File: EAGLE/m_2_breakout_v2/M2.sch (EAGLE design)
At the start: 37 parts, among them X1 C-GRID-14-70543, X2 C-GRID-14-70543, X4 87758-0416

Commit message: Fixed everything about m2 board, just need optional switch rack
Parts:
- removed P_5V, P_ML_EN, P_MR_EN: LSP10, solpad:LSP10
- removed X3: (no value), con-molex:KK-156-2
- added 5V_M2, J_5V_HEX, J_GND_HEX, J_GND_SCH, J_LED_B, J_LED_B_D, J_LED_R, J_LED_R_D, J_ML_OUT1, J_ML_OUT1_D, J_MR_CAPS_GND, J_MR_OUT1, J_MR_OUT1_D, J_MR_PWM, J_MR_PWM_D: ARDUINO_HEADER_1X1_OCTAGON, ben_kramer:ARDUINO_HEADER_1X1_OCTAGON
- added 5V_RAIL: (no value), con-lsta:FE06-1
- added BATTERY, BREAKBEAM_IN: MOLEX_2_PIN, ben_kramer:MOLEX_2_PIN
- added BREAKBEAM_POT: POTENTIOMETER_1, ben_kramer:POTENTIOMETER_1
- added BREAKBEAM_RP: 10k, ben_kramer:RESISTOR_THROUGH_8MM
- added BREAKBEAM_RS: 1k, ben_kramer:RESISTOR_THROUGH_8MM
- added POSITIONING_LED: RGB_LED, ben_kramer:RGB_LED
- renumbered ML_DIODE_NOTE to MR_DIODE_NOT, SV3 to GND_RAIL
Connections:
- net N$3 renamed B5
- net N$6 renamed C7
- removed net GND_1: J_GND5.MP, MWII_L.3
- removed net N$14: C1.2, C2.1, IC1.GND
- removed net N$34: C1.1, C4.1, IC1.IN, X3-2.S, X4-2.S, X4-4.S
- removed net N$5: U$1.C6, X1-5.S
- removed net N$51: C4.2, GND_RAIL.1, GND_RAIL.2, GND_RAIL.3, GND_RAIL.4, GND_RAIL.5, GND_RAIL.6, X3-1.S, X4-1.S, X4-3.S
- new net 5V_HEX: HEX_INVERTER.VCC, J_5V_HEX.1
- new net BREAKBEAM_OUT: BREAKBEAM_IN.2, BREAKBEAM_RP.1, BREAKBEAM_RS.2, U$1.C6, X1-5.S
- new net GND_HEX: HEX_INVERTER.GND, J_GND_HEX.1
- new net GND_SCH: J_GND_SCH.1, SCHMITT_INVERTER.GND
- new net IN_GND: BATTERY.2, C1.2, C2.1, C4.2, GND_RAIL.1, GND_RAIL.2, GND_RAIL.3, GND_RAIL.4, GND_RAIL.5, GND_RAIL.6, IC1.GND, X4-1.S, X4-3.S
- new net LED_B: J_LED_B.1, POSITIONING_LED.B
- new net LED_R: J_LED_R.1, POSITIONING_LED.R
- new net M2_GND: BREAKBEAM_IN.1, BREAKBEAM_RP.2, J_GND5.MP, MWII_L.3
- new net ML_OUT1_D: J_ML_OUT1_D.1, TO_MOTOR_CONTROLLER.2
- new net MR_CAPS_GND: J_MR_CAPS_GND.1, MR_CAP.1, MR_CAP_NOT.1
- new net MR_OUT1_D: J_MR_OUT1_D.1, TO_MOTOR_CONTROLLER.5
- new net MR_PWM_D: HEX_INVERTER.6A, J_MR_PWM_D.1
- new net N$19: 5V_M2.1, U$1.V+, X1-1.S
- new net N$6: BREAKBEAM_POT.2, BREAKBEAM_RS.1
- new net VIN: BATTERY.1, C1.1, C4.1, IC1.IN, X4-2.S, X4-4.S
- net 5V: now also 5V_RAIL.1, 5V_RAIL.2, 5V_RAIL.3, 5V_RAIL.4, 5V_RAIL.5, 5V_RAIL.6, BREAKBEAM_POT.1; no longer HEX_INVERTER.VCC, P_5V.MP, U$1.V+, X1-1.S
- net B2: now also J_LED_B_D.1
- net B3: now also J_LED_R_D.1
- net GND: no longer HEX_INVERTER.GND, MR_CAP.1, MR_CAP_NOT.1, SCHMITT_INVERTER.GND
- net ML_EN: no longer P_ML_EN.MP
- net ML_OUT1: now also J_ML_OUT1.1; no longer TO_MOTOR_CONTROLLER.2
- net MR_EN: no longer P_MR_EN.MP
- net MR_OUT1: now also J_MR_OUT1.1; no longer TO_MOTOR_CONTROLLER.5
- net MR_PWM: now also J_MR_PWM.1; no longer HEX_INVERTER.6A
- net N$17: now also POSITIONING_LED.GND

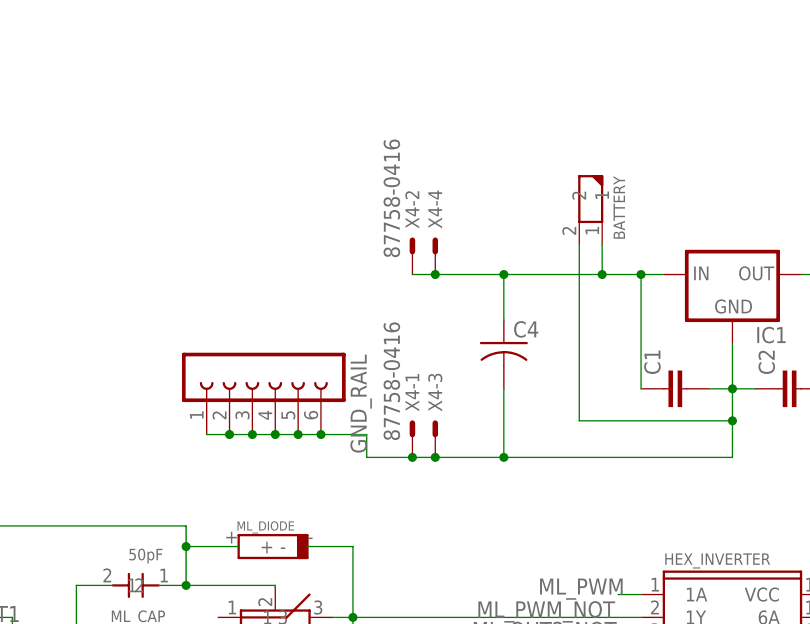
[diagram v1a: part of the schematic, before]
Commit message: Fixed headers out
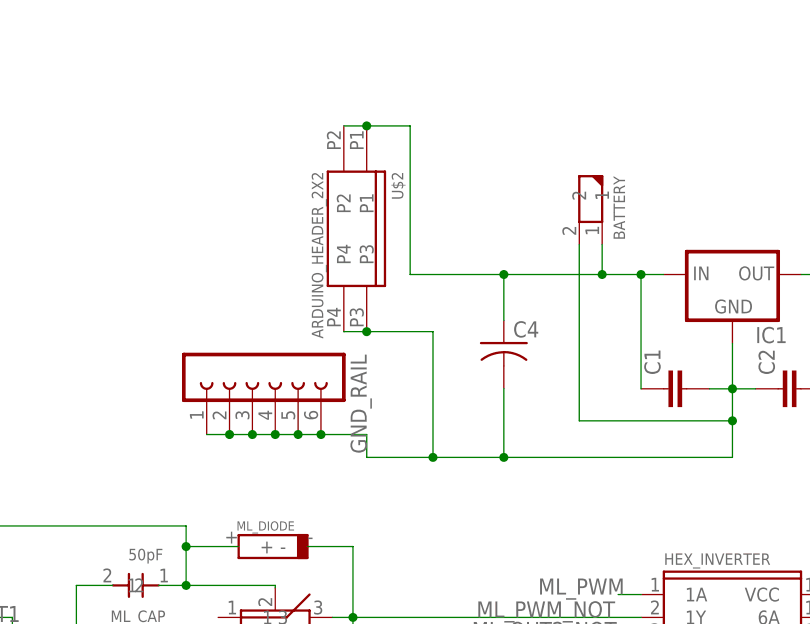
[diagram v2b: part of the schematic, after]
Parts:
- removed X4: 87758-0416, con-molex:87758-0416
- added U$2: ARDUINO_HEADER_2X2, ben_kramer:ARDUINO_HEADER_2X2
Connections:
- net IN_GND: now also U$2.P3, U$2.P4; no longer X4-1.S, X4-3.S
- net VIN: now also U$2.P1, U$2.P2; no longer X4-2.S, X4-4.S
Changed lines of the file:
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@@
 <part name="C2" library="capacitor-wima" deviceset="C" device="2,5-3"/>
 <part name="IC1" library="v-reg" deviceset="78MXXS" device=""/>
-<part name="X4" library="con-molex" deviceset="87758-0416" device=""/>
 <part name="MWII_L" library="con-lstb" deviceset="MA03-1" device=""/>
 <part name="MWII_R" library="con-lstb" deviceset="MA03-1" device=""/>
@@
 <part name="BREAKBEAM_RS" library="ben_kramer" deviceset="RESISTOR_THROUGH_8MM" device="" value="1k"/>
 <part name="BREAKBEAM_POT" library="ben_kramer" deviceset="POTENTIOMETER_1" device=""/>
+<part name="U$2" library="ben_kramer" deviceset="ARDUINO_HEADER_2X2" device=""/>
 </parts>
 <sheets>
@@
 <instance part="C2" gate="G$1" x="12.7" y="78.74" rot="R90"/>
 <instance part="IC1" gate="A" x="7.62" y="91.44"/>
-<instance part="X4" gate="-1" x="-27.94" y="73.66" rot="R90"/>
-<instance part="X4" gate="-2" x="-27.94" y="93.98" rot="R90"/>
-<instance part="X4" gate="-3" x="-25.4" y="73.66" rot="R90"/>
-<instance part="X4" gate="-4" x="-25.4" y="93.98" rot="R90"/>
 <instance part="MWII_L" gate="G$1" x="129.54" y="50.8" rot="R90"/>
 <instance part="MWII_R" gate="G$1" x="129.54" y="45.72" rot="R270"/>
@@
 <instance part="BREAKBEAM_RS" gate="G$1" x="-25.4" y="-20.32"/>
 <instance part="BREAKBEAM_POT" gate="G$1" x="-35.56" y="-27.94"/>
+<instance part="U$2" gate="G$1" x="-33.02" y="96.52" rot="R270"/>
 </instances>
 <busses>
@@
 <wire x1="-2.54" y1="78.74" x2="-2.54" y2="91.44" width="0.1524" layer="91"/>
 <junction x="-2.54" y="91.44"/>
-<pinref part="X4" gate="-4" pin="S"/>
 <wire x1="-2.54" y1="91.44" x2="-6.858" y2="91.44" width="0.1524" layer="91"/>
-<pinref part="X4" gate="-2" pin="S"/>
 <wire x1="-6.858" y1="91.44" x2="-17.78" y2="91.44" width="0.1524" layer="91"/>
-<wire x1="-17.78" y1="91.44" x2="-25.4" y2="91.44" width="0.1524" layer="91"/>
-<wire x1="-25.4" y1="91.44" x2="-27.94" y2="91.44" width="0.1524" layer="91"/>
-<junction x="-25.4" y="91.44"/>
+<wire x1="-17.78" y1="91.44" x2="-28.194" y2="91.44" width="0.1524" layer="91"/>
 <junction x="-17.78" y="91.44"/>
 <wire x1="-17.78" y1="91.44" x2="-17.78" y2="86.36" width="0.1524" layer="91"/>
@@
 <wire x1="-6.858" y1="94.742" x2="-6.858" y2="91.44" width="0.1524" layer="91"/>
 <junction x="-6.858" y="91.44"/>
+<pinref part="U$2" gate="G$1" pin="P2"/>
+<pinref part="U$2" gate="G$1" pin="P1"/>
+<wire x1="-35.56" y1="107.95" x2="-33.02" y2="107.95" width="0.1524" layer="91"/>
+<wire x1="-33.02" y1="107.95" x2="-28.194" y2="107.95" width="0.1524" layer="91"/>
+<wire x1="-28.194" y1="107.95" x2="-28.194" y2="91.44" width="0.1524" layer="91"/>
+<junction x="-33.02" y="107.95"/>
 </segment>
 </net>
@@
 <junction x="-38.1" y="73.66"/>
 <wire x1="-17.78" y1="71.12" x2="7.62" y2="71.12" width="0.1524" layer="91"/>
-<pinref part="X4" gate="-3" pin="S"/>
-<pinref part="X4" gate="-1" pin="S"/>
-<wire x1="-17.78" y1="71.12" x2="-25.4" y2="71.12" width="0.1524" layer="91"/>
-<wire x1="-25.4" y1="71.12" x2="-27.94" y2="71.12" width="0.1524" layer="91"/>
-<junction x="-25.4" y="71.12"/>
 <wire x1="-17.78" y1="78.74" x2="-17.78" y2="71.12" width="0.1524" layer="91"/>
 <junction x="-17.78" y="71.12"/>
 <pinref part="C4" gate="G$1" pin="2"/>
-<wire x1="-33.02" y1="71.12" x2="-27.94" y2="71.12" width="0.1524" layer="91"/>
-<junction x="-27.94" y="71.12"/>
+<wire x1="-33.02" y1="71.12" x2="-25.654" y2="71.12" width="0.1524" layer="91"/>
+<wire x1="-25.654" y1="71.12" x2="-17.78" y2="71.12" width="0.1524" layer="91"/>
 <wire x1="7.62" y1="75.184" x2="7.62" y2="71.12" width="0.1524" layer="91"/>
 <junction x="7.62" y="75.184"/>
-</segment>
-</net>
+<pinref part="U$2" gate="G$1" pin="P4"/>
+<pinref part="U$2" gate="G$1" pin="P3"/>
+<wire x1="-35.56" y1="85.09" x2="-33.02" y2="85.09" width="0.1524" layer="91"/>
+<wire x1="-33.02" y1="85.09" x2="-25.654" y2="85.09" width="0.1524" layer="91"/>
+<wire x1="-25.654" y1="85.09" x2="-25.654" y2="71.12" width="0.1524" layer="91"/>
+<junction x="-33.02" y="85.09"/>
+<junction x="-25.654" y="71.12"/>
+</segment>
+</net>

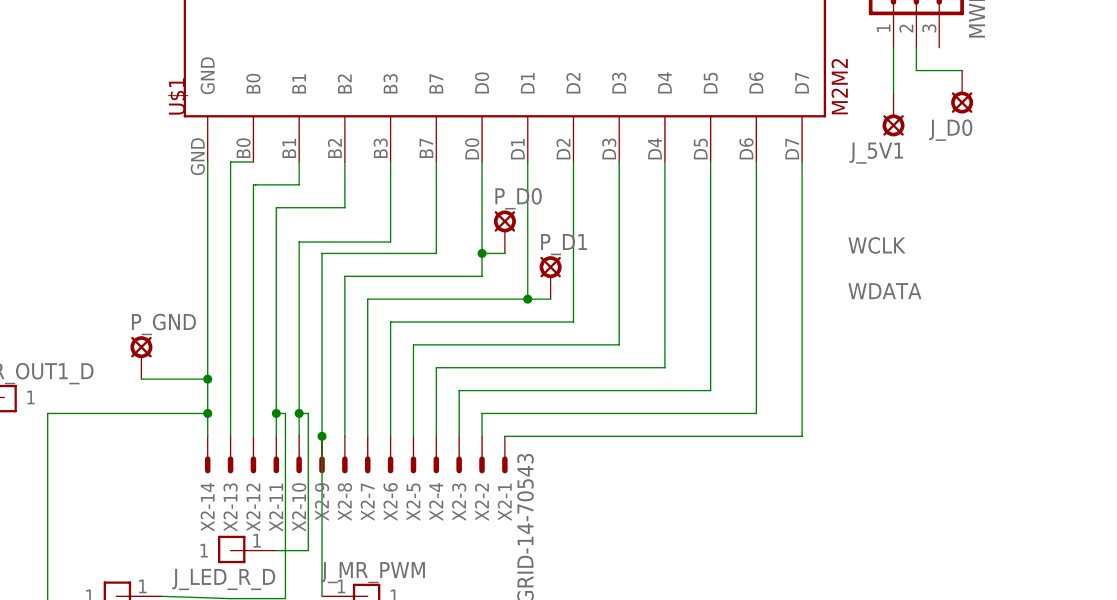
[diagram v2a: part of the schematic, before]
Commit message: Added switch for rink side
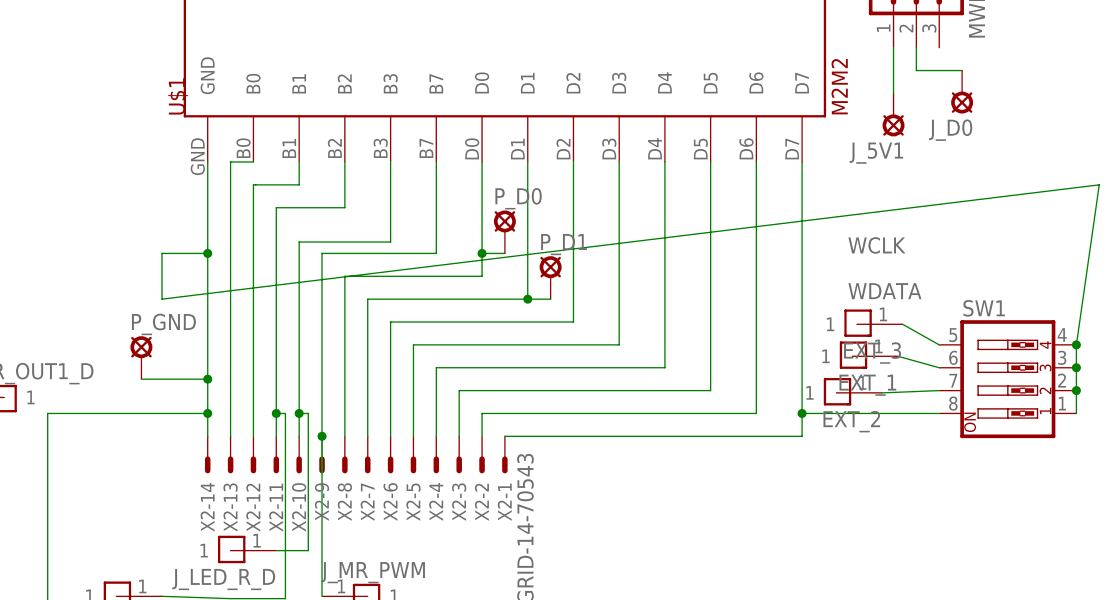
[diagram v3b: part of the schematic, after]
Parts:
- added EXT_1, EXT_2, EXT_3: ARDUINO_HEADER_1X1_OCTAGON, ben_kramer:ARDUINO_HEADER_1X1_OCTAGON
- added SW1: (no value), special:SW_DIP-4
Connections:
- removed net N$17: POSITIONING_LED.GND, P_GND.MP, U$1.GND, X2-14.S
- new net N$14: EXT_1.1, SW1.6
- new net N$16: EXT_3.1, SW1.5
- new net N$3: POSITIONING_LED.GND, P_GND.MP, SW1.1, SW1.2, SW1.3, SW1.4, U$1.GND, X2-14.S
- new net N$5: EXT_2.1, SW1.7
- net N$29: now also SW1.8
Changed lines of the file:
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@@
 <?xml version="1.0" encoding="utf-8"?>
 <!DOCTYPE eagle SYSTEM "eagle.dtd">
-<eagle version="7.2.0">
+<eagle version="7.7.0">
 <drawing>
 <settings>
@@
 <setting verticaltext="up"/>
 </settings>
-<grid distance="0.1" unitdist="inch" unit="inch" style="lines" multiple="1" display="no" altdistance="0.01" altunitdist="inch" altunit="inch"/>
+<grid distance="0.01" unitdist="inch" unit="inch" style="lines" multiple="1" display="no" altdistance="0.01" altunitdist="inch" altunit="inch"/>
 <layers>
 <layer number="1" name="Top" color="4" fill="1" visible="no" active="no"/>
@@
 <part name="BREAKBEAM_POT" library="ben_kramer" deviceset="POTENTIOMETER_1" device=""/>
 <part name="U$2" library="ben_kramer" deviceset="ARDUINO_HEADER_2X2" device=""/>
+<part name="SW1" library="special" deviceset="SW_DIP-4" device=""/>
+<part name="EXT_3" library="ben_kramer" deviceset="ARDUINO_HEADER_1X1_OCTAGON" device=""/>
+<part name="EXT_1" library="ben_kramer" deviceset="ARDUINO_HEADER_1X1_OCTAGON" device=""/>
+<part name="EXT_2" library="ben_kramer" deviceset="ARDUINO_HEADER_1X1_OCTAGON" device=""/>
 </parts>
 <sheets>
@@
 <instance part="BREAKBEAM_POT" gate="G$1" x="-35.56" y="-27.94"/>
 <instance part="U$2" gate="G$1" x="-33.02" y="96.52" rot="R270"/>
+<instance part="SW1" gate="A" x="139.7" y="2.54"/>
+<instance part="EXT_3" gate="G$1" x="122.936" y="7.366" rot="R180"/>
+<instance part="EXT_1" gate="G$1" x="122.428" y="3.81" rot="R180"/>
+<instance part="EXT_2" gate="G$1" x="120.65" y="-0.254" rot="R180"/>
 </instances>
 <busses>
@@
 <segment>
 <pinref part="U$1" gate="G$1" pin="D7"/>
-<wire x1="116.84" y1="25.4" x2="116.84" y2="-5.08" width="0.1524" layer="91"/>
+<wire x1="116.84" y1="25.4" x2="116.84" y2="-2.54" width="0.1524" layer="91"/>
 <pinref part="X2" gate="-1" pin="S"/>
+<wire x1="116.84" y1="-2.54" x2="116.84" y2="-5.08" width="0.1524" layer="91"/>
 <wire x1="116.84" y1="-5.08" x2="83.82" y2="-5.08" width="0.1524" layer="91"/>
+<pinref part="SW1" gate="A" pin="8"/>
+<wire x1="132.08" y1="-2.54" x2="116.84" y2="-2.54" width="0.1524" layer="91"/>
+<junction x="116.84" y="-2.54"/>
 </segment>
 </net>
@@
 <pinref part="P_D0" gate="1" pin="MP"/>
 <label x="121.92" y="15.24" size="1.778" layer="95"/>
-</segment>
-</net>
-<net name="N$17" class="1">
-<segment>
-<pinref part="X2" gate="-14" pin="S"/>
-<pinref part="P_GND" gate="1" pin="MP"/>
-<pinref part="U$1" gate="G$1" pin="GND"/>
-<wire x1="50.8" y1="25.4" x2="50.8" y2="1.27" width="0.1524" layer="91"/>
-<wire x1="50.8" y1="1.27" x2="43.434" y2="1.27" width="0.1524" layer="91"/>
-<junction x="50.8" y="1.27"/>
-<wire x1="50.8" y1="1.27" x2="50.8" y2="-2.54" width="0.1524" layer="91"/>
-<wire x1="50.8" y1="-2.54" x2="50.8" y2="-5.08" width="0.1524" layer="91"/>
-<wire x1="50.8" y1="-2.54" x2="33.02" y2="-2.54" width="0.1524" layer="91"/>
-<wire x1="33.02" y1="-2.54" x2="33.02" y2="-33.02" width="0.1524" layer="91"/>
-<junction x="50.8" y="-2.54"/>
-<pinref part="POSITIONING_LED" gate="G$1" pin="GND"/>
 </segment>
 </net>
@@
 </segment>
 </net>
+<net name="N$3" class="0">
+<segment>
+<pinref part="SW1" gate="A" pin="1"/>
+<pinref part="SW1" gate="A" pin="2"/>
+<wire x1="147.32" y1="-2.54" x2="147.32" y2="0" width="0.1524" layer="91"/>
+<pinref part="SW1" gate="A" pin="3"/>
+<wire x1="147.32" y1="0" x2="147.32" y2="2.54" width="0.1524" layer="91"/>
+<junction x="147.32" y="0"/>
+<pinref part="SW1" gate="A" pin="4"/>
+<wire x1="147.32" y1="2.54" x2="147.32" y2="5.08" width="0.1524" layer="91"/>
+<junction x="147.32" y="2.54"/>
+<wire x1="147.32" y1="5.08" x2="149.86" y2="22.86" width="0.1524" layer="91"/>
+<junction x="147.32" y="5.08"/>
+<wire x1="149.86" y1="22.86" x2="45.72" y2="10.16" width="0.1524" layer="91"/>
+<wire x1="45.72" y1="10.16" x2="45.72" y2="15.24" width="0.1524" layer="91"/>
+<pinref part="X2" gate="-14" pin="S"/>
+<pinref part="P_GND" gate="1" pin="MP"/>
+<pinref part="U$1" gate="G$1" pin="GND"/>
+<wire x1="50.8" y1="25.4" x2="50.8" y2="15.24" width="0.1524" layer="91"/>
+<wire x1="50.8" y1="15.24" x2="50.8" y2="1.27" width="0.1524" layer="91"/>
+<wire x1="50.8" y1="1.27" x2="43.434" y2="1.27" width="0.1524" layer="91"/>
+<junction x="50.8" y="1.27"/>
+<wire x1="50.8" y1="1.27" x2="50.8" y2="-2.54" width="0.1524" layer="91"/>
+<wire x1="50.8" y1="-2.54" x2="50.8" y2="-5.08" width="0.1524" layer="91"/>
+<wire x1="50.8" y1="-2.54" x2="33.02" y2="-2.54" width="0.1524" layer="91"/>
+<wire x1="33.02" y1="-2.54" x2="33.02" y2="-33.02" width="0.1524" layer="91"/>
+<junction x="50.8" y="-2.54"/>
+<pinref part="POSITIONING_LED" gate="G$1" pin="GND"/>
+<wire x1="45.72" y1="15.24" x2="50.8" y2="15.24" width="0.1524" layer="91"/>
+<junction x="50.8" y="15.24"/>
+</segment>
+</net>
+<net name="N$5" class="0">
+<segment>
+<pinref part="SW1" gate="A" pin="7"/>
+<wire x1="132.08" y1="0" x2="125.73" y2="-0.254" width="0.1524" layer="91"/>
+<pinref part="EXT_2" gate="G$1" pin="1"/>
+</segment>
+</net>
+<net name="N$14" class="0">
+<segment>
+<pinref part="SW1" gate="A" pin="6"/>
+<wire x1="132.08" y1="2.54" x2="127.508" y2="3.81" width="0.1524" layer="91"/>
+<pinref part="EXT_1" gate="G$1" pin="1"/>
+</segment>
+</net>
+<net name="N$16" class="0">
+<segment>
+<pinref part="SW1" gate="A" pin="5"/>
+<pinref part="EXT_3" gate="G$1" pin="1"/>
+<wire x1="132.08" y1="5.08" x2="128.016" y2="7.366" width="0.1524" layer="91"/>
+</segment>
+</net>
